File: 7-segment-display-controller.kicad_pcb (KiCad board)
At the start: 4 copper layers, 71 x 54 mm, 54 parts, among them J101 Tag Connector, J102 USB_B_Micro, J103 JST 2.54 Header, J104 JST 2.54 Header, Q101 AO3501A, SW101 SW_DIP_x04, SW102 SW_Push, SW103 SW_Push, SW104 SW_Push, SW105 SW_Push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

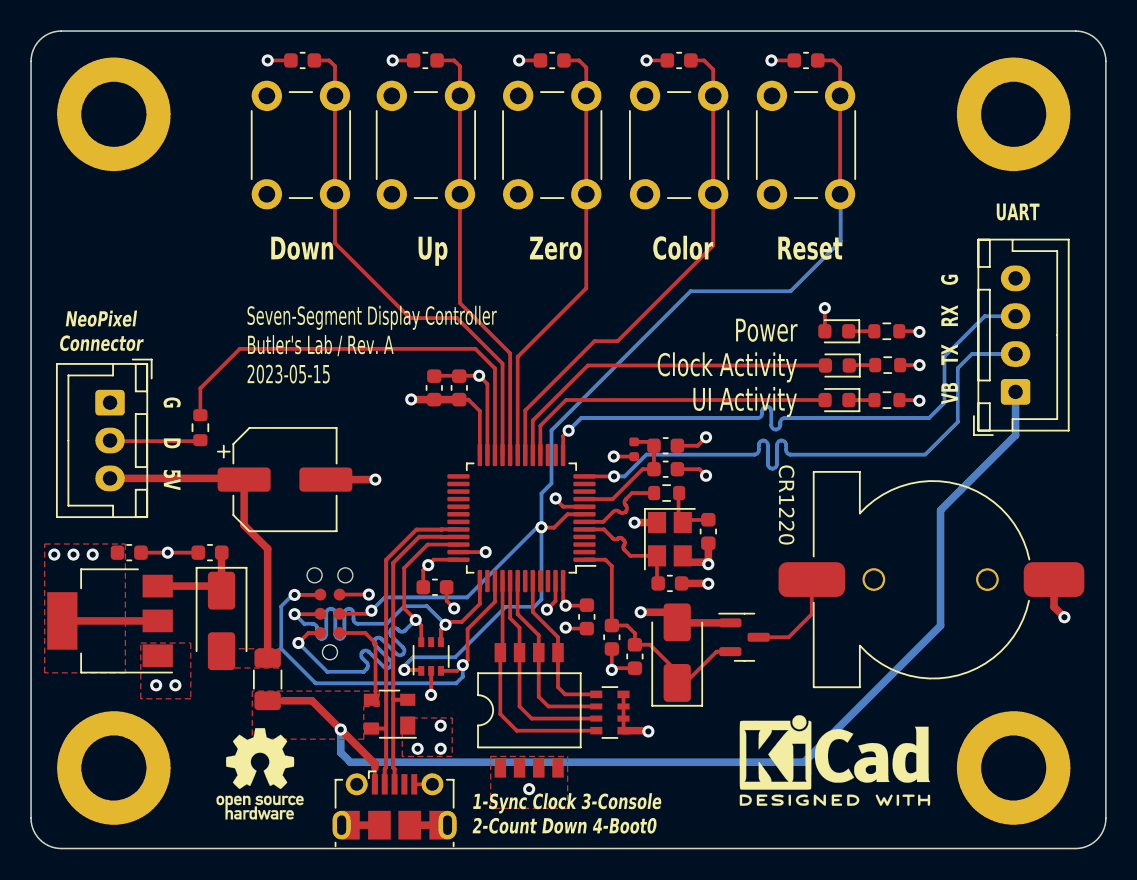
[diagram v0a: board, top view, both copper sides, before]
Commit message: add alternate power source connector
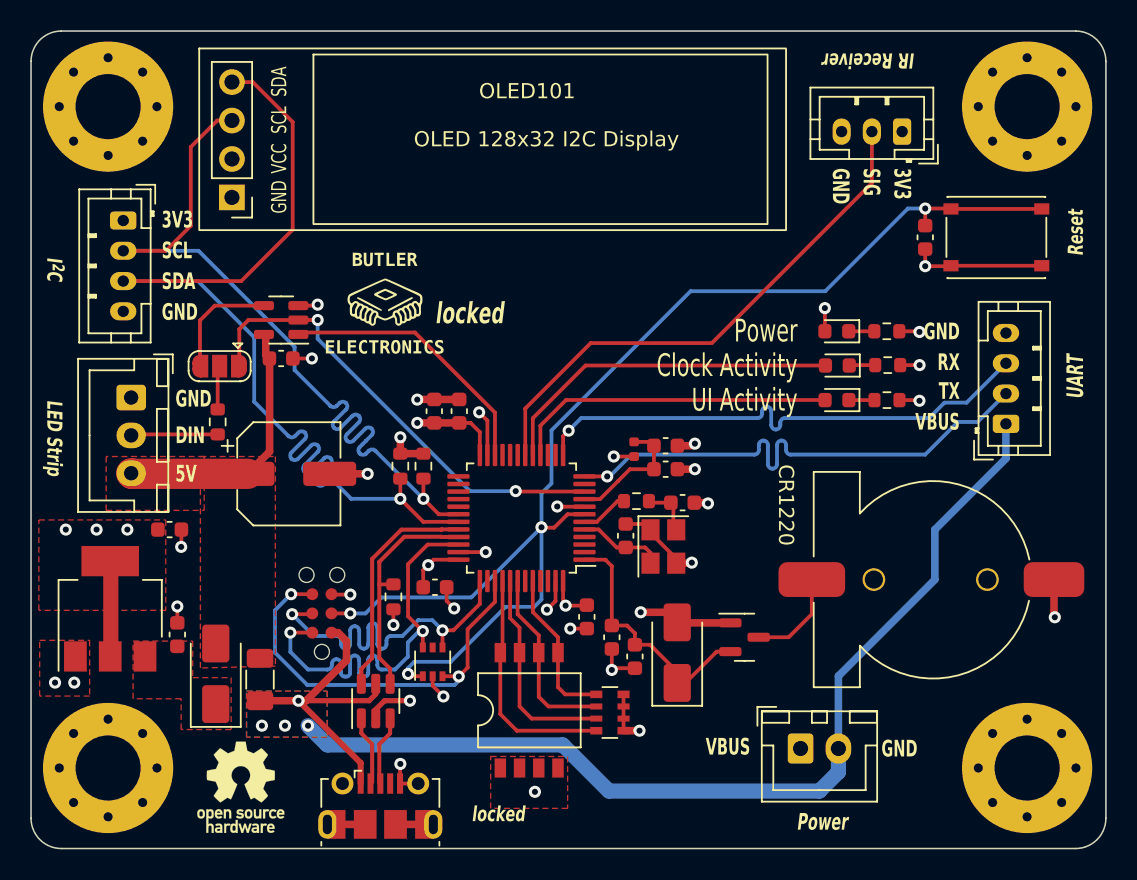
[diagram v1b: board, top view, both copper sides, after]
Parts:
- removed C110, C111, C112, C113: 100nF, Capacitor_SMD:C_0603_1608Metric
- removed D105: SP0503BAHT, User_Footprint:SOT-143-4
- removed the REF** at (125.2, 83.1)
- removed SW102, SW103, SW104, SW105: SW_Push, Button_Switch_THT:SW_PUSH_6mm
- added C118: 100nF, Capacitor_SMD:C_0603_1608Metric, F.Cu at (88.6, 56.5)
- added G***: LOGO, User_Footprint:butler-electronics-10, F.Cu at (95.5, 52.8)
- added J105: JST 2.54 Header, Connector_JST:JST_PH_B4B-PH-K_1x04_P2.00mm_Vertical, F.Cu at (78.2, 47.4)
- added J106: JST 2.54 Header, Connector_JST:JST_PH_B3B-PH-K_1x03_P2.00mm_Vertical, F.Cu at (129.7, 41.5)
- added J107: Conn_01x02, Connector_JST:JST_XH_B2B-XH-A_1x02_P2.50mm_Vertical, F.Cu at (123.0, 82.3)
- added OLED101: OLED_I2C, User_Footprint:OLED_128x32_I2C_4pins, F.Cu at (103.0, 42.0)
- added R108: 1K5, Resistor_SMD:R_0603_1608Metric, F.Cu at (96.1, 72.3)
- added R109: 1K5, Resistor_SMD:R_0603_1608Metric, F.Cu at (96.5, 63.6)
- added R110: 1K5, Resistor_SMD:R_0603_1608Metric, F.Cu at (98.0, 63.6)
- added SW107: SW_SPDT, Jumper:SolderJumper-3_P1.3mm_Open_RoundedPad1.0x1.5mm, F.Cu at (84.6, 57.0)
- added U102: USBLC6-2SC6, Package_TO_SOT_SMD:SOT-23-6, F.Cu at (94.9, 79.1)
- added U103: 74AHCT1G125, Package_TO_SOT_SMD:SOT-23-5, F.Cu at (88.6, 54.0)
- H101, H102, H103, H104: footprint MountingHole:MountingHole_4.3mm_M4_DIN965_Pad -> MountingHole:MountingHole_4.3mm_M4_Pad_Via
- J103: footprint Connector_JST:JST_XH_B4B-XH-A_1x04_P2.50mm_Vertical -> Connector_JST:JST_PH_B4B-PH-K_1x04_P2.00mm_Vertical
- SW106: footprint Button_Switch_THT:SW_PUSH_6mm -> User_Footprint:XKB-Connectivity-TS-1187A-B-A-B
- moved C114 14.1 mm to (131.2, 48.5), turned to -90 degrees
- moved SW106 13.9 mm to (135.9, 48.5), turned to 0 degrees
- moved C201 5.83 mm to (81.8, 74.8), turned to -90 degrees
- moved C108 4.30 mm to (111.4, 68.2), turned to 90 degrees
- moved D103 3.51 mm to (84.3, 77.3), turned to 90 degrees
- moved C202 3.07 mm to (81.3, 67.8)
- moved C109 2.55 mm to (115.2, 66.0), turned to 0 degrees
- moved J103 2.21 mm to (136.5, 60.8)
- moved R103 2.06 mm to (112.1, 65.9)
- moved REF** 1.55 mm to (86.0, 84.8)
- moved C102 1.54 mm to (98.8, 60.0)
- moved C103 1.54 mm to (100.4, 60.0)
- moved J104 1.44 mm to (78.7, 59.1)
- moved R104 1.20 mm to (84.5, 60.7)
- moved H101 1.02 mm to (137.9, 39.9)
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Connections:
- H101 pad 1: (no net) -> GND
- H102 pad 1: (no net) -> GND
- H103 pad 1: (no net) -> GND
- H104 pad 1: (no net) -> GND
- J102 pad 2: /D_N -> /USB_D_N
- J102 pad 3: /D_P -> /USB_D_P
- R104 pad 2: /LED_PIXEL -> Net-(SW107-B)
- U101 pad 10: unconnected-(U101-PA0-Pad10) -> /RGB_LED
- U101 pad 18: /RGB_COLOR -> /IR_RECV
- U101 pad 19: /CLK_RST -> unconnected-(U101-PB1-Pad19)
- U101 pad 20: /CLK_UP -> unconnected-(U101-PB2-Pad20)
- U101 pad 21: /CLK_DN -> unconnected-(U101-PB10-Pad21)
- U101 pad 22: /LED_PIXEL -> /~{OE}
- U101 pad 30: unconnected-(U101-PA9-Pad30) -> /SCL
- U101 pad 31: unconnected-(U101-PA10-Pad31) -> /SDA
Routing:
- net /SDA: track 0.00 -> 66.4 mm, vias 0 -> 1
- net /SCL: track 0.00 -> 53.7 mm, vias 0 -> 1
- net /IR_RECV: track 0.00 -> 35.5 mm
- net /CLK_DN: track 33.6 -> 0.00 mm
- net /RGB_COLOR: track 33.2 -> 0.00 mm
- net /RGB_LED: track 0.00 -> 30.9 mm, vias 0 -> 2
- net /CLK_RST: track 29.1 -> 0.00 mm
- net /CLK_UP: track 28.7 -> 0.00 mm
- net /LED_PIXEL: track 28.6 -> 0.00 mm
- net /~{OE}: track 0.00 -> 18.0 mm
- net VBUS: track 78.2 -> 87.4 mm, vias 1 -> 4
- net Net-(SW107-C): track 0.00 -> 7.65 mm
- net /LDO_3V3/5V: track 6.86 -> 0.22 mm
- net /D_N: track 21.5 -> 15.1 mm
- net /D_P: track 20.7 -> 15.2 mm
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- added copper zone on F.Cu, net /LDO_3V3/5V
- added copper zone on B.Cu, net VBUS
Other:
- board text added: "3V3"
- board text added: "DIN"
- board text added: "GND"
- board text added: "IR Receiver"
- board text added: "I^{2}C"
- board text added: "LED Strip"
- board text added: "NRST"
- board text added: "SCL"
- board text added: "SDA"
- board text added: "SIG"
- board text added: "SWCLK"
- board text added: "SWDIO"
- board text added: "SWO"
- board text added: "VBUS"
- board text added: "locked"
- board text removed: "${TITLE} ${COMPANY} / Rev. ${REVISION} ${ISSUE_DATE}"
- board text removed: "1-Sync Clock 3-Console 2-Count Down 4-Boot0"
- board text removed: "Color"
- board text removed: "D"
- board text removed: "Down"
- board text removed: "G"
- board text removed: "NeoPixel Connector"
- board text removed: "Up"
- board text removed: "VB"
- board text removed: "Zero"

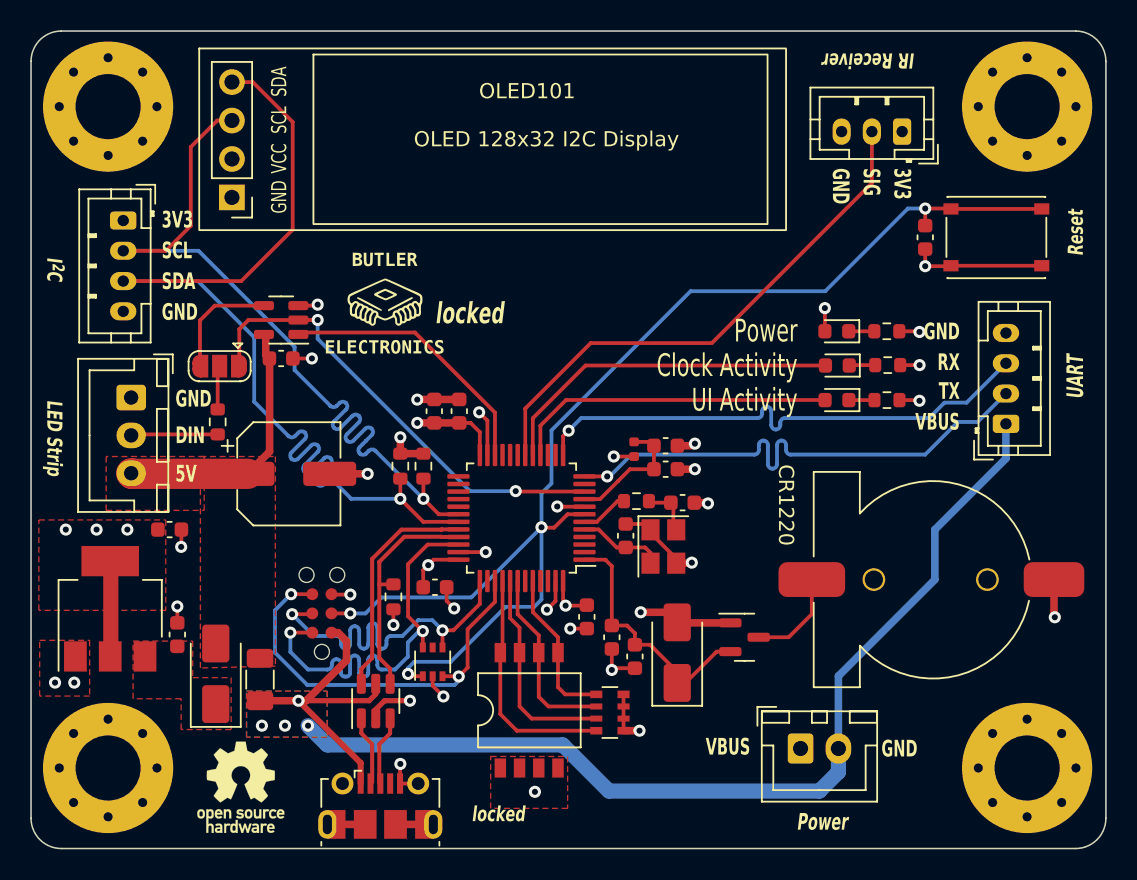
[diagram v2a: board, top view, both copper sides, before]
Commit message: fix crystal pin assignments
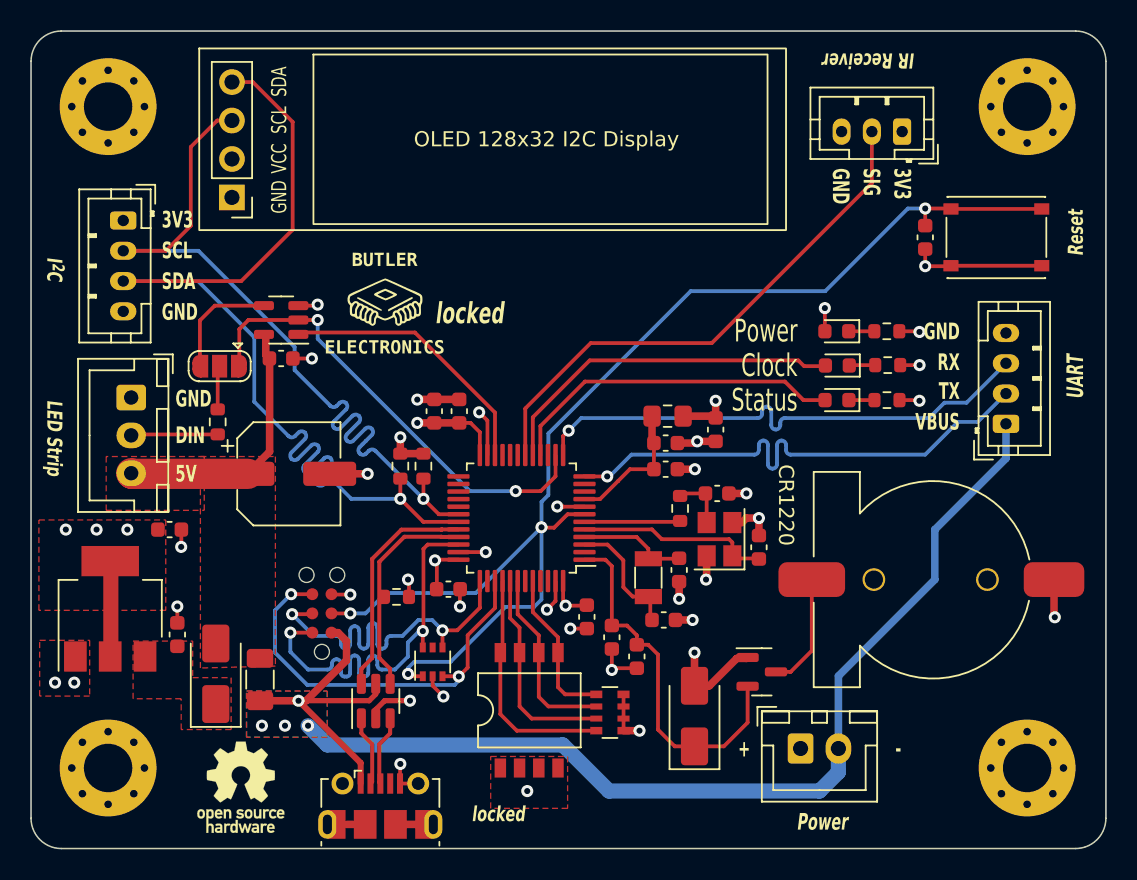
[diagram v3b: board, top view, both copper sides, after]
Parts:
- added C110: 1uF, Capacitor_SMD:C_0603_1608Metric, F.Cu at (117.3, 61.2)
- added C112: 15pF, Capacitor_SMD:C_0603_1608Metric, F.Cu at (113.9, 73.8)
- added C113: 15pF, Capacitor_SMD:C_0603_1608Metric, F.Cu at (114.9, 70.5)
- added Y103: 32.768kHz, Crystal:Crystal_SMD_3215-2Pin_3.2x1.5mm, F.Cu at (112.9, 71.0)
- FB101: renamed from L101; value 39nH -> 600@100MHz; footprint Inductor_SMD:L_0402_1005Metric -> Inductor_SMD:L_0805_2012Metric_Pad1.15x1.40mm_HandSolder
- H101, H102, H103, H104: footprint MountingHole:MountingHole_4.3mm_M4_Pad_Via -> MountingHole:MountingHole_3.2mm_M3_Pad_Via
- moved C108 8.83 mm to (120.2, 69.0)
- moved D106 4.34 mm to (116.0, 80.1)
- moved Y101 3.74 mm to (117.6, 68.5), turned to 90 degrees
- moved FB101 3.11 mm to (114.2, 60.3), turned to 0 degrees
- moved R103 2.92 mm to (115.0, 66.4), turned to 90 degrees
- moved Q101 2.56 mm to (120.4, 77.2)
- moved C109 2.37 mm to (117.4, 65.4)
- moved C104 0.90 mm to (99.7, 71.8)
- moved R108 0.20 mm to (96.3, 72.3), turned to 0 degrees
- moved C107 0.18 mm to (114.0, 62.1)
- moved C101 0.13 mm to (112.1, 76.2)
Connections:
- U101 pad 10: /RGB_LED -> unconnected-(U101-PA0-Pad10)
- U101 pad 14: unconnected-(U101-PA4-Pad14) -> /RGB_LED
- U101 pad 3: unconnected-(U101-PC14-Pad3) -> /LSE_IN
- U101 pad 4: unconnected-(U101-PC15-Pad4) -> /LSE_OUT
- Y101 pad 1: GND -> /HSE_IN
- Y101 pad 2: /HSE_IN -> GND
- Y101 pad 3: GND -> Net-(C109-Pad1)
- Y101 pad 4: Net-(C109-Pad1) -> GND
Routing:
- net /LSE_IN: track 0.00 -> 8.33 mm
- net /VBAT: track 17.0 -> 24.5 mm
- net /LSE_OUT: track 0.00 -> 7.24 mm
- net /HSE_IN: track 5.68 -> 12.9 mm
- net /HSE_OUT: track 3.17 -> 6.34 mm
- net GND: track 64.6 -> 67.0 mm, vias 29 -> 32
- net +3V3: track 31.8 -> 33.9 mm
- net /BAT+: track 6.43 -> 7.64 mm
- net /LED_UI: track 21.4 -> 22.4 mm
- net /D_P: track 15.2 -> 14.3 mm
- net /SWDIO: track 28.7 -> 27.9 mm
- net +3.3VA: track 8.37 -> 8.96 mm
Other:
- board text added: "+"
- board text added: "-"
- board text added: "Clock"
- board text added: "Status"
- board text removed: "Clock Activity"
- board text removed: "UI Activity"

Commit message: switch MCU to STM32F401
- switch MCU to STM32F401 because STM32F303 does not have DMA stream
- add EEPROM
- removed D+ pull-up resistor
- switch status LED to blue, changed resistor values
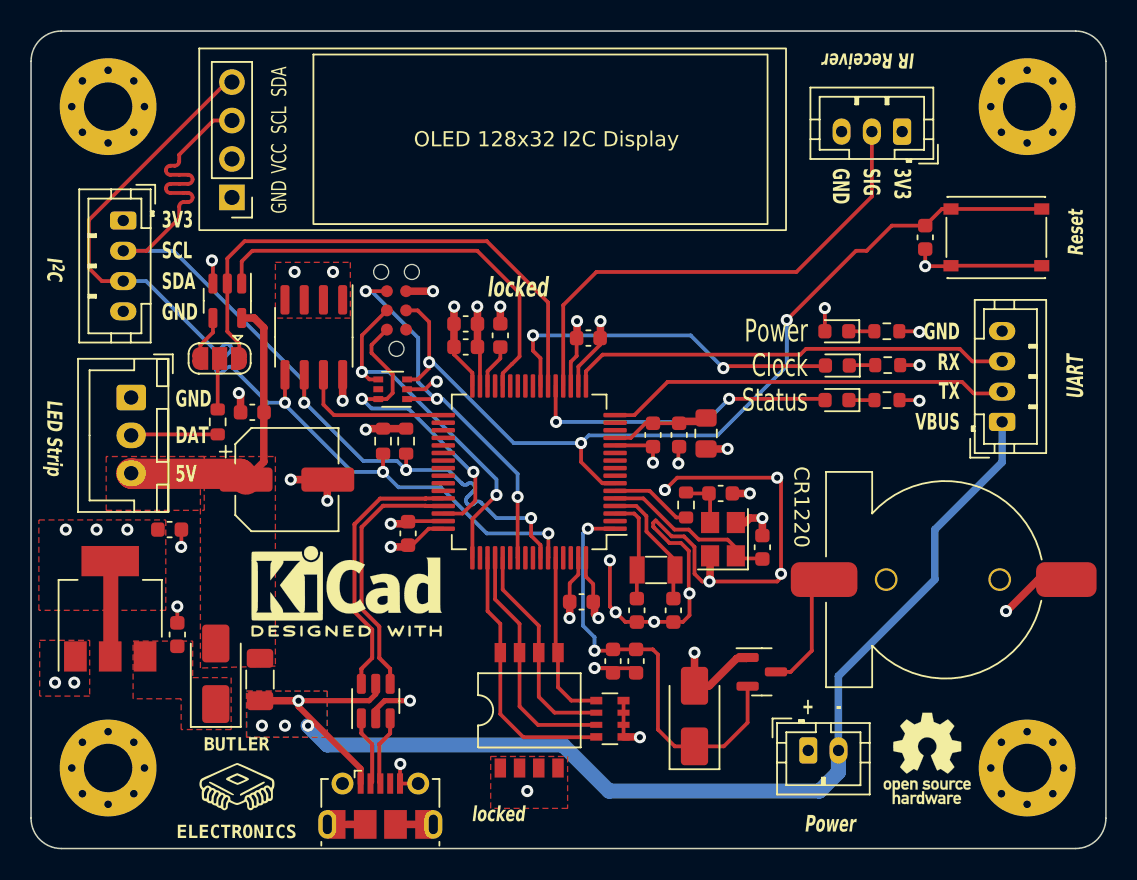
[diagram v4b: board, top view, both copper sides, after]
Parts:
- removed C110: 1uF, Capacitor_SMD:C_0603_1608Metric
- removed R108: 1K5, Resistor_SMD:R_0603_1608Metric
- added C111: 100nF, Capacitor_SMD:C_0603_1608Metric, F.Cu at (108.9, 55.2)
- added C117: 4.7uF, Capacitor_SMD:C_0603_1608Metric, F.Cu at (103.1, 55.0)
- added REF**: KiCad-Logo2_5mm_SilkScreen, Symbol:KiCad-Logo2_5mm_SilkScreen, F.Cu at (93.0, 71.9)
- added U104: M24C64-RMN, Package_SO:SOIC-8_3.9x4.9mm_P1.27mm, F.Cu at (90.8, 55.1)
- C106: value 10nF -> 100nF
- D107: value GREEN -> BLUE
- J107: footprint Connector_JST:JST_XH_B2B-XH-A_1x02_P2.50mm_Vertical -> Connector_JST:JST_PH_B2B-PH-K_1x02_P2.00mm_Vertical
- R101, R105: value 1K5 -> 2K2
- R103: value 47 -> 0
- U101: value STM32F303CBT6 -> STM32F401RCTx; footprint Package_QFP:LQFP-48_7x7mm_P0.5mm -> Package_QFP:LQFP-64_10x10mm_P0.5mm
- moved REF** 45.4 mm to (131.3, 82.9)
- moved G*** 33.5 mm to (85.7, 84.8)
- moved J101 20.6 mm to (96.3, 53.3)
- moved D104 18.2 mm to (96.0, 58.5), turned to 180 degrees
- moved C102 6.13 mm to (100.8, 54.2), turned to 0 degrees
- moved C104 4.55 mm to (97.0, 68.1), turned to 90 degrees
- moved C103 4.26 mm to (100.8, 55.8), turned to 0 degrees
- moved C118 4.03 mm to (86.7, 60.1), turned to 180 degrees
- moved U103 3.78 mm to (85.1, 52.7), turned to -90 degrees
- moved U101 3.09 mm to (105.0, 64.0)
- moved FB101 2.79 mm to (116.7, 61.5), turned to -90 degrees
- moved C113 2.69 mm to (114.6, 73.2)
- moved C106 2.41 mm to (113.2, 61.6), turned to -90 degrees
- moved R109 2.01 mm to (95.4, 62.0)
- moved R110 2.01 mm to (96.9, 62.0)
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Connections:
- D104 pad 1: /NRST -> /SWO
- D104 pad 3: /SWO -> /NRST
- J101 pad 1: VBUS -> unconnected-(J101-Pin_1-Pad1)
- U101 pad 12: /UART_TX -> GND
- U101 pad 13: /UART_RX -> +3.3VA
- U101 pad 14: /RGB_LED -> unconnected-(U101-PA0-Pad14)
- U101 pad 16: /LED_UI -> /UART_TX
- U101 pad 17: /LED_HB -> /UART_RX
- U101 pad 18: /IR_RECV -> GND
- U101 pad 19: unconnected-(U101-PB1-Pad19) -> +3V3
- U101 pad 20: unconnected-(U101-PB2-Pad20) -> /IR_RECV
- U101 pad 21: unconnected-(U101-PB10-Pad21) -> /LED_UI
- U101 pad 22: /~{OE} -> /RGB_LED
- U101 pad 23: GND -> /LED_HB
- U101 pad 24: +3V3 -> unconnected-(U101-PC4-Pad24)
- U101 pad 28: unconnected-(U101-PB15-Pad28) -> /~{OE}
- U101 pad 30: /SCL -> Net-(U101-VCAP1)
- U101 pad 31: /SDA -> GND
- U101 pad 32: /D_N -> +3V3
- U101 pad 33: /D_P -> /~{EEPROM}
- U101 pad 34: /SWDIO -> unconnected-(U101-PB13-Pad34)
- U101 pad 35: GND -> unconnected-(U101-PB14-Pad35)
- U101 pad 36: +3V3 -> unconnected-(U101-PB15-Pad36)
- U101 pad 37: /SWCLK -> unconnected-(U101-PC6-Pad37)
- U101 pad 39: /SWO -> unconnected-(U101-PC8-Pad39)
- U101 pad 40: /DIP3 -> unconnected-(U101-PC9-Pad40)
- U101 pad 41: /DIP2 -> unconnected-(U101-PA8-Pad41)
- U101 pad 42: /DIP1 -> unconnected-(U101-PA9-Pad42)
- U101 pad 44: /BOOT0 -> /D_N
- U101 pad 45: unconnected-(U101-PB8-Pad45) -> /D_P
- U101 pad 46: unconnected-(U101-PB9-Pad46) -> /SWDIO
- U101 pad 8: GND -> unconnected-(U101-PC0-Pad8)
- U101 pad 9: +3.3VA -> unconnected-(U101-PC1-Pad9)
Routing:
- net GND: track 67.0 -> 119.5 mm, vias 32 -> 38
- net /NRST: track 82.6 -> 61.6 mm, vias 4 -> 3
- net /~{EEPROM}: track 0.00 -> 10.2 mm
- net /~{OE}: track 18.0 -> 27.9 mm
- net /UART_TX: track 34.6 -> 26.8 mm, vias 1 -> 0
- net /SCL: track 53.7 -> 61.3 mm, vias 1 -> 3
- net VBUS: track 87.4 -> 80.6 mm
- net /SWDIO: track 27.9 -> 21.2 mm
- net /UART_RX: track 34.7 -> 29.4 mm, vias 1 -> 0
- net +3V3: track 33.9 -> 38.9 mm, vias 12 -> 13
- net /RGB_LED: track 30.8 -> 35.8 mm, vias 2 -> 0
- net /SDA: track 66.4 -> 61.6 mm, vias 1 -> 3
- net Net-(SW107-C): track 7.65 -> 3.03 mm
- net /VBAT: track 24.5 -> 29.1 mm, vias 0 -> 2
- net Net-(U101-VCAP1): track 0.00 -> 2.92 mm
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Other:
- board text added: "DAT"
- board text removed: "DIN"
